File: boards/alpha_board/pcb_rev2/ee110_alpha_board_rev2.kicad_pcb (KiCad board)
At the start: 2 copper layers, 90 parts, among them J1 power, J2 Conn_ARM_JTAG_SWD_10, J3 keypad, J4 Micro_SD_Card, J5 SERVO1, J6 SERVO2, SW1 RESET, SW2 TEST_BUTTON, U1 TLV76150DCY, U10 MPU-9250, U2 TLV76133DCY, U3 NC7SZ08M5X, U4 LM3724EM5-4.63/NOPB, U5 CC2652, U6 74LS138, U7 74LVC245, U8 LM386, U9 LM2902, X1 48MHz, X2 32.768KHz

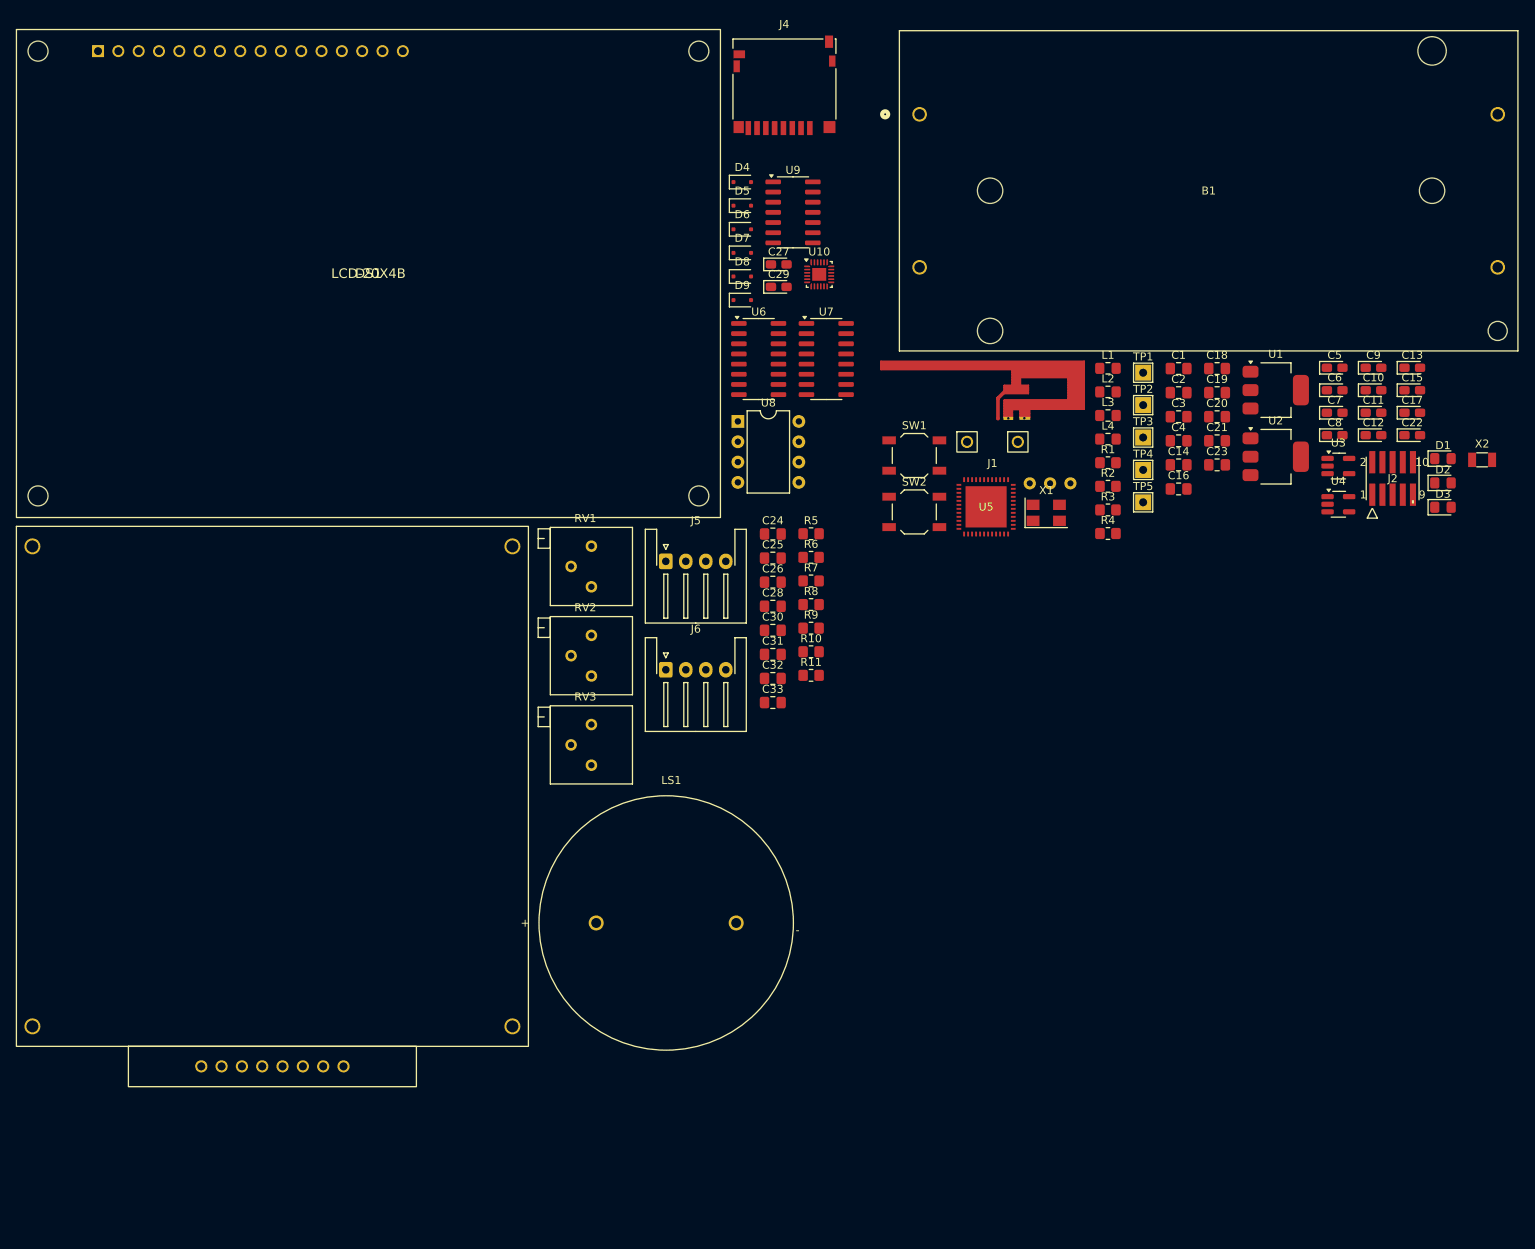
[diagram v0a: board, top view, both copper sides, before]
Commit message: split body-back, body-top and body-front into smaller parts
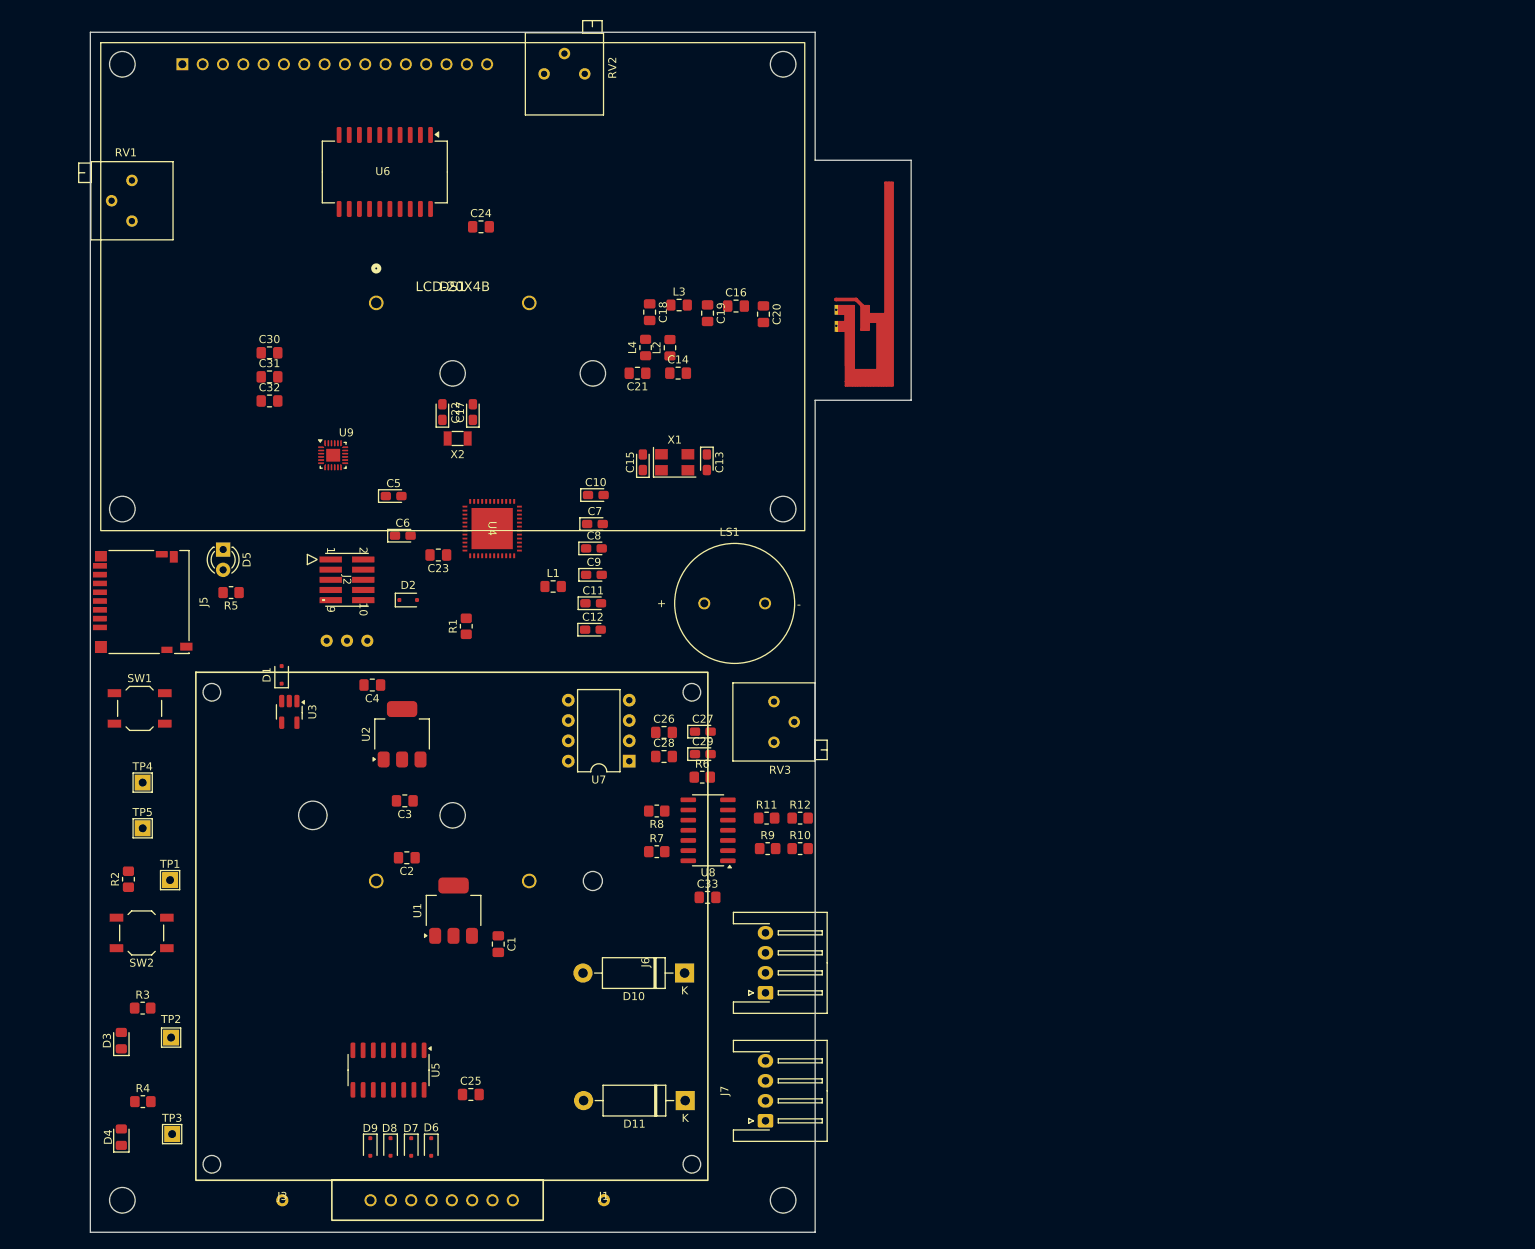
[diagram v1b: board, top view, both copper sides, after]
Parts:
- removed the U3 at (206.7, 82.3)
- added D1: D_Small_Filled, Diode_SMD:D_SOD-323F, F.Cu at (74.6, 108.4)
- added D2: D_Small_Filled, Diode_SMD:D_SOD-323F, F.Cu at (90.4, 99.0)
- added J4: keypad, Alpha Board rev2 library:4x4_Keypad, F.Cu at (95.9, 140.6)
- added R1: 4.7k, Resistor_SMD:R_0805_2012Metric_Pad1.20x1.40mm_HandSolder, F.Cu at (97.7, 102.3)
- added REF**: MountingHole_3.2mm_M3_DIN965, MountingHole:MountingHole_3.2mm_M3_DIN965, F.Cu at (137.3, 174.1)
- added REF**: MountingHole_3.2mm_M3_DIN965, MountingHole:MountingHole_3.2mm_M3_DIN965, F.Cu at (54.7, 174.1)
- B1: moved to B.Cu
- D10: renamed from D8; footprint Diode_SMD:D_SOD-323F -> Diode_THT:D_DO-15_P12.70mm_Horizontal
- D11: renamed from D9; footprint Diode_SMD:D_SOD-323F -> Diode_THT:D_DO-15_P12.70mm_Horizontal
- D5: renamed from D3; footprint LED_SMD:LED_0805_2012Metric_Pad1.15x1.40mm_HandSolder -> LED_THT:LED_D3.0mm
- J1: value power -> POWER; footprint Alpha Board rev2 library:My_Power_Connector -> My_Footprint:1pin
- J3: value keypad -> GND; footprint Alpha Board rev2 library:4x4_Keypad -> My_Footprint:1pin
- LS1: footprint Alpha Board rev2 library:CUI_CVS-3108 -> Alpha Board rev2 library:SPKR_CVS-1508
- R5: renamed from R4; value 200 -> 280
- U6: renamed from U7; footprint Package_SO:SOIC-16_3.9x9.9mm_P1.27mm -> Package_SO:SOIC-20W_7.5x15.4mm_P1.27mm
- moved D4 184.3 mm to (54.6, 166.2), turned to 90 degrees
- moved D3 180.5 mm to (54.6, 154.1), turned to 90 degrees
- moved D5 152.6 mm to (67.3, 92.7), turned to -90 degrees
- moved TP3 149.4 mm to (60.9, 165.8)
- moved TP2 145.0 mm to (60.8, 153.7)
- moved R4 141.5 mm to (57.2, 161.7)
- moved TP1 137.2 mm to (60.6, 134.0)
- moved R3 137.2 mm to (57.2, 150.0)
- moved U3 133.7 mm to (75.5, 113.0), turned to -90 degrees
- moved R2 133.0 mm to (55.4, 133.9), turned to 90 degrees
- moved TP5 131.5 mm to (57.2, 127.6)
- moved J2 131.3 mm to (82.8, 96.5), turned to -90 degrees
- moved TP4 131.0 mm to (57.2, 121.9)
- moved X2 128.1 mm to (96.6, 78.8), turned to 180 degrees
- moved D6 126.7 mm to (93.3, 167.4), turned to -90 degrees
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- renumbered D1 to D3, D2 to D4, D4 to D6, D5 to D7, D6 to D8, D7 to D9, J4 to J5, J5 to J6, J6 to J7, R9 to R10, R10 to R11, R11 to R12, R1 to R2, R2 to R3, R3 to R4, R5 to R6, R6 to R7, R7 to R8, R8 to R9, U4 to U3, U5 to U4, U6 to U5, U8 to U7, U9 to U8, U10 to U9
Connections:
- D10 pad 1: Net-(D8-K) (its old number) -> Net-(D10-K)
- D11 pad 1: Net-(D9-K) (its old number) -> Net-(D11-K)
- D6 pad 2: Net-(D4-A) (its old number) -> Net-(D6-A)
- D7 pad 2: Net-(D5-A) (its old number) -> Net-(D7-A)
- D8 pad 2: Net-(D6-A) -> Net-(D8-A)
- D9 pad 2: Net-(D7-A) -> Net-(D9-A)
- J3 pad 1: Net-(D7-A) -> GND
- J6 pad 2: Net-(J5-Pad2) -> Net-(D10-K)
- J6 pad 4: Net-(D8-K) (its old number) -> Net-(J6-Pad4)
- J7 pad 2: Net-(J6-Pad2) -> Net-(D11-K)
- J7 pad 4: Net-(D9-K) (its old number) -> Net-(J7-Pad4)
- R11 pad 1: Net-(J6-Pad2) -> Net-(J7-Pad4)
- R5 pad 1: +3.3V -> +5V
- R9 pad 1: Net-(J5-Pad2) -> Net-(J6-Pad4)
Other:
- board outline added: 102.6 x 150 mm

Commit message: 4/27
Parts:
- removed TP5: GND, TestPoint:TestPoint_THTPad_2.0x2.0mm_Drill1.0mm
- added REF**: WALL-E, Alpha Board rev2 library:WALL-E, B.Cu at (96.3, 47.2)
- added SW3: SW_SPDT, Alpha Board rev2 library:EG1903, B.Cu at (99.9, 58.5)
- J2: value Conn_ARM_JTAG_SWD_10 -> JTAG
- U1: value TLV76150DCY -> TLV1117-5.0
- U2: value TLV76133DCY -> TLV1117-3.3
- U3: value LM3724EM5-4.63/NOPB -> LM3724
- U9: footprint Package_DFN_QFN:QFN-24-1EP_3x3mm_P0.4mm_EP1.75x1.6mm -> Alpha Board rev2 library:QFN-24-1EP_3x3mm_P0.4mm_EP1.75x1.6mm
- moved R12 25.8 mm to (116.8, 138.7), turned to 180 degrees
- moved TP4 25.6 mm to (74.6, 103.1)
- moved C33 24.9 mm to (105.4, 125.4), turned to 90 degrees
- moved C2 24.6 mm to (80.9, 154.0), turned to 0 degrees
- moved R6 22.0 mm to (114.0, 103.6), turned to -90 degrees
- moved C30 21.7 mm to (80.3, 88.6), turned to -90 degrees
- moved C12 21.4 mm to (113.4, 81.3), turned to 90 degrees
- moved D1 21.1 mm to (95.7, 109.2), turned to 0 degrees
- moved C29 20.3 mm to (107.6, 113.1), turned to 90 degrees
- moved R10 19.6 mm to (120.4, 135.2), turned to 180 degrees
- moved R11 18.9 mm to (121.0, 138.7), turned to 180 degrees
- moved U1 18.5 mm to (80.6, 147.9), turned to 180 degrees
- moved L2 18.4 mm to (109.3, 79.6), turned to 180 degrees
- moved C28 17.2 mm to (116.3, 102.6), turned to 90 degrees
- moved C14 16.7 mm to (108.4, 76.3), turned to 90 degrees
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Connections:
- B1 pad 1: Net-(B1-Pad1) -> Net-(SW3-B)
- B1 pad 3: Net-(B1-Pad1) -> Net-(SW3-A)
- R2 pad 2: /TEST_BUTTON -> /gpio/TEST_BUTTON
- R3 pad 2: /TEST_GREEN -> /gpio/TEST_GREEN
- R4 pad 2: /TEST_BLUE -> /gpio/TEST_BLUE
- RV3 pad 1: /gpio/SPKR -> GND
- RV3 pad 3: GND -> /gpio/SPKR
- TP1 pad 1: /TEST_BUTTON -> /gpio/TEST_BUTTON
- TP2 pad 1: /TEST_GREEN -> /gpio/TEST_GREEN
- TP3 pad 1: /TEST_BLUE -> /gpio/TEST_BLUE
- U4 pad 32: /TEST_BUTTON_1 -> /gpio/TEST_BUTTON
- U4 pad 36: /TEST_GREEN_1 -> /gpio/TEST_GREEN
- U4 pad 37: /TEST_BLUE_1 -> /gpio/TEST_BLUE
- U4 pad 38: /gpio/SPKR -> /gpio/VBAT_READ
- U4 pad 39: /gpio/VBAT_READ -> /gpio/SERVO1_POS
- U4 pad 41: /gpio/SERVO1_POS -> /gpio/SERVO1_PWM
- U4 pad 43: /gpio/SERVO1_PWM -> /gpio/SPKR
- U7 pad 6: +5V -> +3.3V
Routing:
- net GND: track 0.00 -> 356.6 mm, vias 0 -> 205
- net +3.3V: track 0.00 -> 310.1 mm, vias 0 -> 19
- net +5V: track 0.00 -> 222.6 mm
- net +VBAT: track 0.00 -> 96.7 mm
- net /gpio/TEST_BLUE: track 0.00 -> 94.4 mm, vias 0 -> 4
- net /gpio/LCD_RW: track 0.00 -> 90.7 mm, vias 0 -> 2
- net /gpio/TEST_GREEN: track 0.00 -> 88.7 mm, vias 0 -> 4
- net /gpio/SERVO2_PWM: track 0.00 -> 85.1 mm, vias 0 -> 2
- net /gpio/KEYPAD_COL1: track 0.00 -> 83.6 mm, vias 0 -> 2
- net /gpio/KEYPAD_COL2: track 0.00 -> 82.8 mm, vias 0 -> 2
- net /gpio/KEYPAD_COL3: track 0.00 -> 81.9 mm, vias 0 -> 2
- net /gpio/KEYPAD_COL4: track 0.00 -> 81.1 mm, vias 0 -> 2
- net /gpio/KEYPAD_ROWB: track 0.00 -> 79.6 mm, vias 0 -> 2
- net /gpio/KEYPAD_ROWA: track 0.00 -> 78.7 mm, vias 0 -> 4
- net /gpio/TEST_BUTTON: track 0.00 -> 74.9 mm, vias 0 -> 4
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- added copper zone on B.Cu, net GND
- added copper zone on F.Cu, net GND
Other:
- board text added: "Backlight"
- board text added: "Contrast"
- board text added: "EE 110 Alpha Board Adam Krivka v1.0.0"
- board text added: "Volume"
- board text added: "buffer"
